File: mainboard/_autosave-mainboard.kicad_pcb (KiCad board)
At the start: 2 copper layers, 5 parts, among them U1 ESP32-WROOM-32, U2 tps63070, U3 tps63070, U4 tps63070, U5 CP2102N-A01-GQFN24

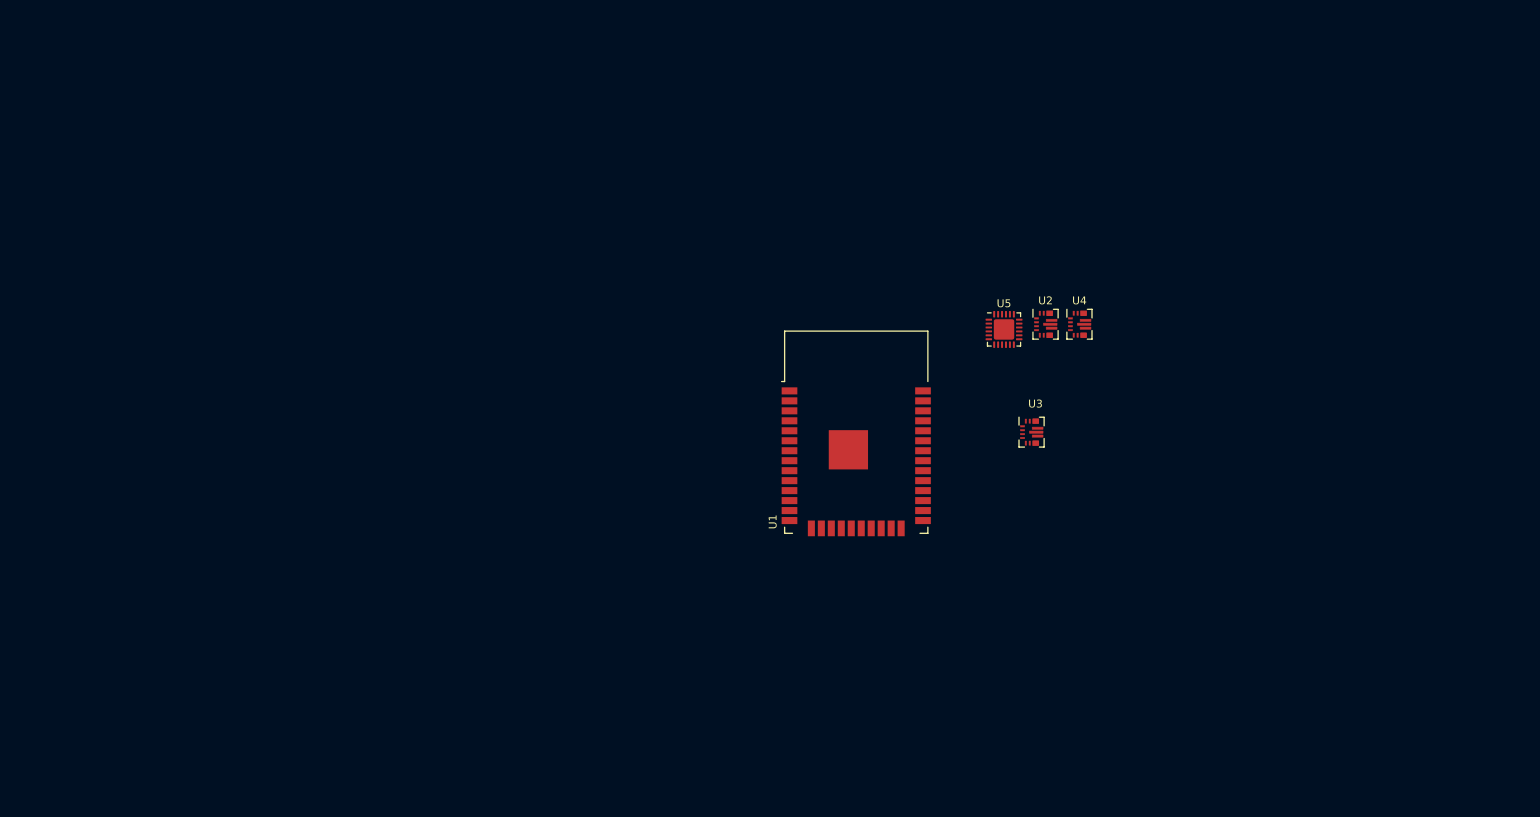
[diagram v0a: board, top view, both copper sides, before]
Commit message: Add sensors
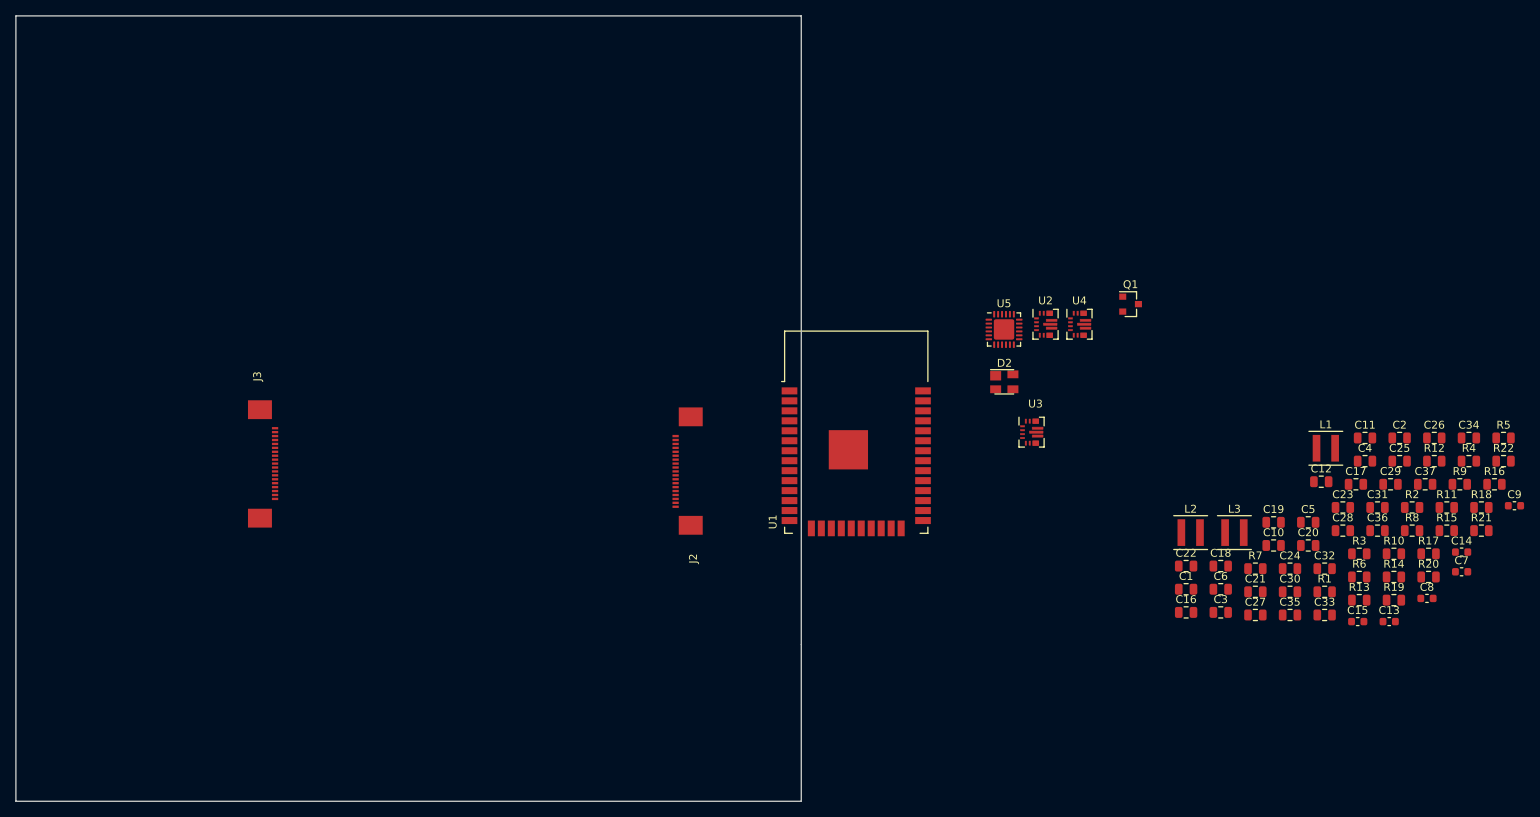
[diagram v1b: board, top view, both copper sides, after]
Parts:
- added C1: C, Capacitor_SMD:C_0805_2012Metric, F.Cu at (179.0, 103.0)
- added C10: 100 nC, Capacitor_SMD:C_0805_2012Metric, F.Cu at (190.1, 97.4)
- added C11: 100 nC, Capacitor_SMD:C_0805_2012Metric, F.Cu at (201.8, 83.7)
- added C12: 100 nC, Capacitor_SMD:C_0805_2012Metric, F.Cu at (196.2, 89.3)
- added C13: C, Capacitor_SMD:C_0603_1608Metric, F.Cu at (204.9, 107.1)
- added C14: C, Capacitor_SMD:C_0603_1608Metric, F.Cu at (214.1, 98.3)
- added C15: C, Capacitor_SMD:C_0603_1608Metric, F.Cu at (200.8, 107.1)
- added C16: C, Capacitor_SMD:C_0805_2012Metric, F.Cu at (179.0, 106.0)
- added C17: C, Capacitor_SMD:C_0805_2012Metric, F.Cu at (200.6, 89.6)
- added C18: C, Capacitor_SMD:C_0805_2012Metric, F.Cu at (183.4, 100.0)
- added C19: C, Capacitor_SMD:C_0805_2012Metric, F.Cu at (190.1, 94.5)
- added C2: C, Capacitor_SMD:C_0805_2012Metric, F.Cu at (206.2, 83.7)
- added C20: C, Capacitor_SMD:C_0805_2012Metric, F.Cu at (194.6, 97.4)
- added C21: C, Capacitor_SMD:C_0805_2012Metric, F.Cu at (187.8, 103.3)
- added C22: C, Capacitor_SMD:C_0805_2012Metric, F.Cu at (179.0, 100.0)
- added C23: C, Capacitor_SMD:C_0805_2012Metric, F.Cu at (199.0, 92.6)
- added C24: C, Capacitor_SMD:C_0805_2012Metric, F.Cu at (192.2, 100.4)
- added C25: C, Capacitor_SMD:C_0805_2012Metric, F.Cu at (206.2, 86.7)
- added C26: C, Capacitor_SMD:C_0805_2012Metric, F.Cu at (210.6, 83.7)
- added C27: C, Capacitor_SMD:C_0805_2012Metric, F.Cu at (187.8, 106.3)
- added C28: C, Capacitor_SMD:C_0805_2012Metric, F.Cu at (199.0, 95.5)
- added C29: C, Capacitor_SMD:C_0805_2012Metric, F.Cu at (205.0, 89.6)
- added C3: C, Capacitor_SMD:C_0805_2012Metric, F.Cu at (183.4, 106.0)
- added C30: C, Capacitor_SMD:C_0805_2012Metric, F.Cu at (192.2, 103.3)
- added C31: C, Capacitor_SMD:C_0805_2012Metric, F.Cu at (203.4, 92.6)
- added C32: C, Capacitor_SMD:C_0805_2012Metric, F.Cu at (196.6, 100.4)
- added C33: C, Capacitor_SMD:C_0805_2012Metric, F.Cu at (196.6, 106.3)
- added C34: C, Capacitor_SMD:C_0805_2012Metric, F.Cu at (215.0, 83.7)
- added C35: C, Capacitor_SMD:C_0805_2012Metric, F.Cu at (192.2, 106.3)
- added C36: 1 nC, Capacitor_SMD:C_0805_2012Metric, F.Cu at (203.4, 95.5)
- added C37: 1 nC, Capacitor_SMD:C_0805_2012Metric, F.Cu at (209.4, 89.6)
- added C4: C, Capacitor_SMD:C_0805_2012Metric, F.Cu at (201.8, 86.7)
- added C5: C, Capacitor_SMD:C_0805_2012Metric, F.Cu at (194.6, 94.5)
- added C6: C, Capacitor_SMD:C_0805_2012Metric, F.Cu at (183.4, 103.0)
- added C7: C, Capacitor_SMD:C_0603_1608Metric, F.Cu at (214.1, 100.8)
- added C8: C, Capacitor_SMD:C_0603_1608Metric, F.Cu at (209.7, 104.2)
- added C9: C, Capacitor_SMD:C_0603_1608Metric, F.Cu at (220.8, 92.4)
- added D2: SP0503BAHT, Package_TO_SOT_SMD:SOT-143, F.Cu at (155.8, 76.6)
- added J2: Conn_01x19_MountingPin, mainboard:Molex_Easy-On_52746-1971_1x19_P0.5mm_Horizontal, F.Cu at (114.0, 88.0)
- added J3: Conn_01x19_MountingPin, mainboard:Molex_Easy-On_52746-1971_1x19_P0.5mm_Horizontal, F.Cu at (63.0, 87.0)
- added L1: L, Inductor_SMD:L_Coilcraft_XxL4020, F.Cu at (196.8, 85.0)
- added L2: L, Inductor_SMD:L_Coilcraft_XxL4020, F.Cu at (179.6, 95.8)
- added L3: L, Inductor_SMD:L_Coilcraft_XxL4020, F.Cu at (185.2, 95.8)
- added Q1: PMV32UP, Package_TO_SOT_SMD:SOT-23, F.Cu at (171.9, 66.7)
- added R1: 10 kR, Resistor_SMD:R_0805_2012Metric, F.Cu at (196.6, 103.3)
- added R10: 10 kR, Resistor_SMD:R_0805_2012Metric, F.Cu at (205.5, 98.5)
- added R11: 10 kR, Resistor_SMD:R_0805_2012Metric, F.Cu at (212.2, 92.6)
- added R12: 10 kR, Resistor_SMD:R_0805_2012Metric, F.Cu at (210.6, 86.7)
- added R13: 100 mR, Resistor_SMD:R_0805_2012Metric, F.Cu at (201.1, 104.4)
- added R14: 100 mR, Resistor_SMD:R_0805_2012Metric, F.Cu at (205.5, 101.4)
- added R15: 100 kR, Resistor_SMD:R_0805_2012Metric, F.Cu at (212.2, 95.5)
- added R16: 1 kR, Resistor_SMD:R_0805_2012Metric, F.Cu at (218.3, 89.6)
- added R17: 4.7 kR, Resistor_SMD:R_0805_2012Metric, F.Cu at (209.9, 98.5)
- added R18: 470 R, Resistor_SMD:R_0805_2012Metric, F.Cu at (216.6, 92.6)
- added R19: 12 kR, Resistor_SMD:R_0805_2012Metric, F.Cu at (205.5, 104.4)
- added R2: 10 kR, Resistor_SMD:R_0805_2012Metric, F.Cu at (207.8, 92.6)
- added R20: 12 kR, Resistor_SMD:R_0805_2012Metric, F.Cu at (209.9, 101.4)
- added R21: 470 R, Resistor_SMD:R_0805_2012Metric, F.Cu at (216.6, 95.5)
- added R22: 470 R, Resistor_SMD:R_0805_2012Metric, F.Cu at (219.4, 86.7)
- added R3: 10 kR, Resistor_SMD:R_0805_2012Metric, F.Cu at (201.1, 98.5)
- added R4: 470 kR, Resistor_SMD:R_0805_2012Metric, F.Cu at (215.0, 86.7)
- added R5: 150 kR, Resistor_SMD:R_0805_2012Metric, F.Cu at (219.4, 83.7)
- added R6: 470 kR, Resistor_SMD:R_0805_2012Metric, F.Cu at (201.1, 101.4)
- added R7: 120 kR, Resistor_SMD:R_0805_2012Metric, F.Cu at (187.8, 100.4)
- added R8: 470 kR, Resistor_SMD:R_0805_2012Metric, F.Cu at (207.8, 95.5)
- added R9: 120 kR, Resistor_SMD:R_0805_2012Metric, F.Cu at (213.8, 89.6)
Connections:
- net +VDC renamed VBUS
- U1 pad 13: Net-(U1-Pad13) -> /SCLK
- U1 pad 14: Net-(U1-Pad14) -> /SOUT1
- U1 pad 16: Net-(U1-Pad16) -> /SIN0
- U1 pad 25: Net-(U1-Pad25) -> /IO0
- U1 pad 3: Net-(U1-Pad3) -> /EN
- U1 pad 34: Net-(U1-Pad34) -> /RXD
- U1 pad 35: Net-(U1-Pad35) -> /TXD
- U1 pad 8: Net-(U1-Pad8) -> /GSCLK
- U1 pad 9: Net-(U1-Pad9) -> /LAT
- U5 pad 19: Net-(U5-Pad19) -> /RTS
- U5 pad 2: Net-(U5-Pad2) -> GND
- U5 pad 20: Net-(U5-Pad20) -> /RXD
- U5 pad 23: Net-(U5-Pad23) -> /DTR
- U5 pad 25: Net-(U5-Pad25) -> GND
- U5 pad 3: Net-(U5-Pad3) -> /D+
- U5 pad 4: Net-(U5-Pad4) -> /D-
- U5 pad 5: Net-(U5-Pad5) -> Net-(C28-Pad1)
- U5 pad 6: Net-(U5-Pad6) -> Net-(C28-Pad1)
- U5 pad 7: Net-(U5-Pad7) -> VUSB
- U5 pad 8: Net-(U5-Pad8) -> VUSB
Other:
- board outline added: 100 x 100 mm
